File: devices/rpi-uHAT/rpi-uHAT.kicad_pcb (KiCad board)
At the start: 2 copper layers, 65 x 30.5 mm, 36 parts, among them J1 GPIO, J2 JST PH, J3 JST SH, J6 PC FAN HEADER, J7 PC FAN HEADER, U1 CAT24C256, U2 AP2112K-3.3, U3 EMC2101-x-ACZL, U4 TCA9406DC, U5 TPS61170DRV

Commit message: !fixup
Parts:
- removed C7: 10u, Capacitor_SMD:C_0805_2012Metric
- removed C8: 22u, Capacitor_SMD:C_1210_3225Metric
- removed C9: 22n, Capacitor_SMD:C_0805_2012Metric
- removed D1: SS14, Diode_SMD:D_SMA
- removed J7: PC FAN HEADER, Connector:FanPinHeader_1x04_P2.54mm_Vertical
- removed L1: 22u, Inductor_SMD:L_Wuerth_MAPI-4020
- removed R7: 9.76k, Resistor_SMD:R_0603_1608Metric
- removed R8: 92k, Resistor_SMD:R_0603_1608Metric
- removed R9: 10.5k, Resistor_SMD:R_0603_1608Metric
- removed U5: TPS61170DRV, Package_SON:WSON-6-1EP_2x2mm_P0.65mm_EP1x1.6mm
- C2, C3: footprint Capacitor_SMD:C_0603_1608Metric -> Capacitor_SMD:C_0805_2012Metric
- moved R2 22.4 mm to (161.7, 78.5), turned to 180 degrees
- moved R1 16.3 mm to (158.7, 78.5), turned to 0 degrees
- moved C1 14.0 mm to (158.5, 85.5)
- moved JP1 14.0 mm to (155.1, 83.3)
- moved U1 14.0 mm to (160.2, 82.0)
- moved J6 12.8 mm to (108.2, 96.4), turned to 0 degrees
- moved C5 8.47 mm to (119.6, 84.3)
- moved C6 8.47 mm to (119.6, 91.8)
- moved R3 8.47 mm to (122.2, 89.6)
- moved R4 8.47 mm to (122.2, 86.6)
- moved U4 8.47 mm to (119.6, 88.1)
- moved C4 6.47 mm to (111.9, 91.0), turned to -90 degrees
- moved R5 5.78 mm to (116.9, 90.2)
- moved C2 5.47 mm to (125.0, 96.3)
- moved C3 5.47 mm to (119.2, 96.3)
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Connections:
- C3 pad 1: +5V -> +5V_RPI
- J1 pad 1: +5V -> +5V_RPI
- J1 pad 3: +5V -> +5V_RPI
- J2 pad MP: GND -> +3V3
- J3 pad MP: GND -> +3V3
- J6 pad 2: +12V -> +5V_RPI
- U2 pad 1: +5V -> +5V_RPI
- U2 pad 3: +5V -> +5V_RPI
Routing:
- net +5V: track 68.9 -> 0.00 mm, vias 2 -> 0
- net +3V3_RPI: track 92.6 -> 139.1 mm, vias 0 -> 2
- net GND: track 74.4 -> 35.1 mm, vias 47 -> 37
- net /ID_SDA: track 5.44 -> 25.5 mm
- net /FAN: track 26.3 -> 8.36 mm, vias 0 -> 1
- net +12V: track 17.7 -> 0.00 mm
- net /ID_SCL: track 13.6 -> 29.7 mm
- net /SDA: track 61.7 -> 68.6 mm
- net /SCL: track 56.1 -> 62.6 mm
- net +5V_RPI: track 0.00 -> 3.38 mm
- net /FB: track 3.23 -> 0.00 mm
- net /GPIO3/SCL1: track 21.1 -> 18.5 mm, vias 2 -> 0
- net Net-(C9-Pad1): track 1.90 -> 0.00 mm
- net Net-(U5-COMP): track 1.69 -> 0.00 mm
- net /GPIO2/SDA1: track 26.7 -> 25.8 mm, vias 2 -> 0
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- added copper zone on F.Cu, net +5V_RPI
- removed copper zone on F.Cu, net +12V
- removed copper zone on B.Cu, net +3V3
- removed copper zone on F.Cu, net +5V
- removed copper zone on F.Cu, net /SW

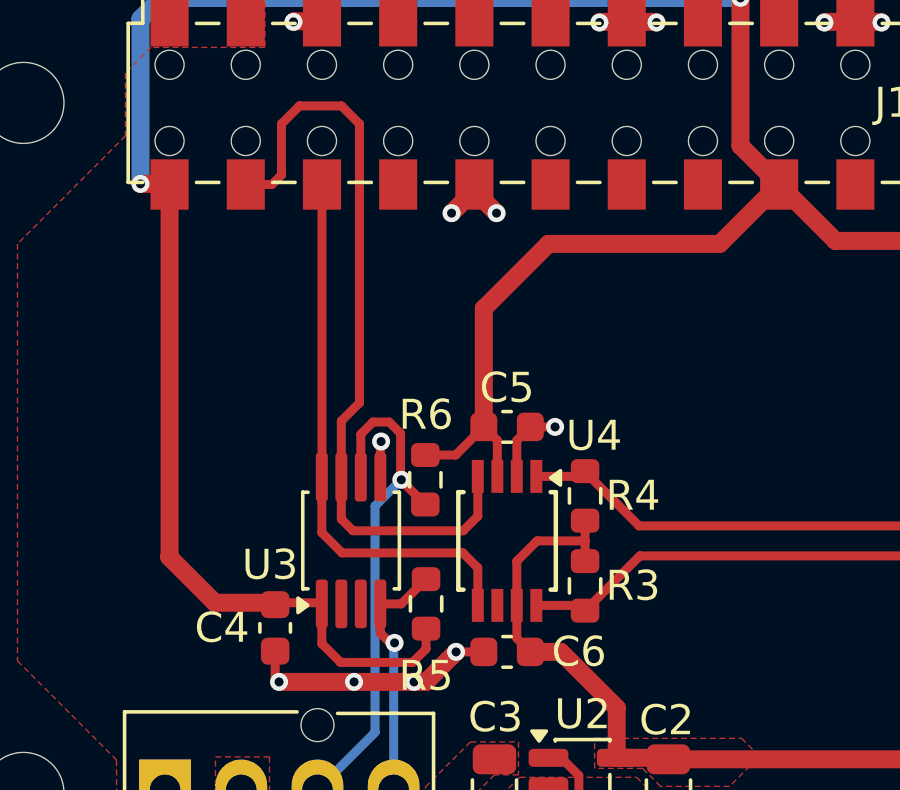
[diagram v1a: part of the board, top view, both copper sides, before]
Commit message: [rpi-uHAT] Adds MPN for all parts.
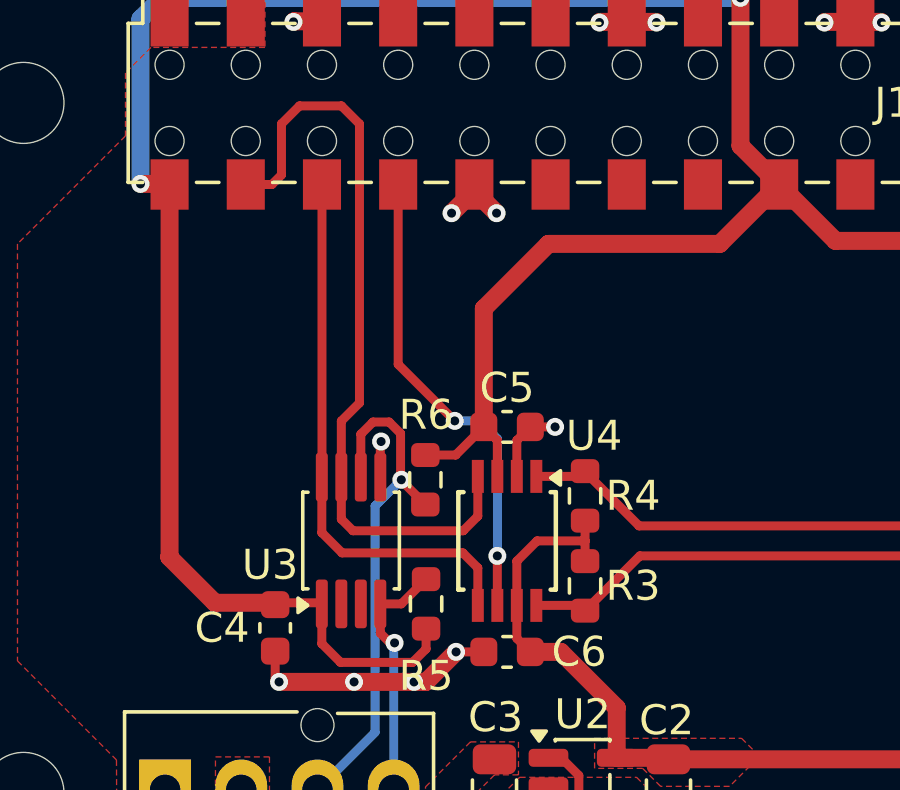
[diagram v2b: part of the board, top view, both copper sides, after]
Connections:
- J1 pad 8: /GPIO4/GPCLK0 -> /EN
- U4 pad 6: unconnected-(U4-OE-Pad6) -> /EN
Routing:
- net /EN: track 0.00 -> 16.2 mm, vias 0 -> 2
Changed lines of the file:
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@@
 			(size 1.27 1.68)
 			(layers "F.Cu" "F.Mask" "F.Paste")
-			(net "/GPIO4{slash}GPCLK0")
+			(net "/EN")
 			(pinfunction "Pin_8_8")
 			(pintype "passive")
@@
 			(size 1.1 0.4)
 			(layers "F.Cu" "F.Mask" "F.Paste")
-			(net "unconnected-(U4-OE-Pad6)")
+			(net "/EN")
 			(pinfunction "OE_6")
 			(pintype "input")
@@
 	)
 	(segment
-		(start 115.99 75.880158)
-		(end 115.99 76.22)
-		(width 0.3)
-		(layer "F.Cu")
-		(net "/GPIO4{slash}GPCLK0")
-	)
-	(segment
 		(start 151.224842 73.015)
 		(end 151.875158 73.015)
@@
 		(net "Net-(JP1-A)")
 	)
+	(segment
+		(start 119.295 88.6)
+		(end 119.295 90.25)
+		(width 0.3)
+		(layer "F.Cu")
+		(net "/EN")
+	)
+	(segment
+		(start 115.99 75.880158)
+		(end 115.99 76.22)
+		(width 0.3)
+		(layer "F.Cu")
+		(net "/EN")
+	)
+	(segment
+		(start 117.875 84.1)
+		(end 115.99 82.215)
+		(width 0.3)
+		(layer "F.Cu")
+		(net "/EN")
+	)
+	(segment
+		(start 115.99 82.215)
+		(end 115.99 76.22)
+		(width 0.3)
+		(layer "F.Cu")
+		(net "/EN")
+	)
+	(via
+		(at 117.875 84.1)
+		(size 0.6)
+		(drill 0.3)
+		(layers "F.Cu" "B.Cu")
+		(net "/EN")
+	)
+	(via
+		(at 119.295 88.6)
+		(size 0.6)
+		(drill 0.3)
+		(layers "F.Cu" "B.Cu")
+		(net "/EN")
+	)
+	(segment
+		(start 119.3 84.7)
+		(end 119.3 88.595)
+		(width 0.3)
+		(layer "B.Cu")
+		(net "/EN")
+	)
+	(segment
+		(start 118.7 84.1)
+		(end 119.3 84.7)
+		(width 0.3)
+		(layer "B.Cu")
+		(net "/EN")
+	)
+	(segment
+		(start 117.875 84.1)
+		(end 118.7 84.1)
+		(width 0.3)
+		(layer "B.Cu")
+		(net "/EN")
+	)
+	(segment
+		(start 119.3 88.595)
+		(end 119.295 88.6)
+		(width 0.3)
+		(layer "B.Cu")
+		(net "/EN")
+	)
 	(zone
